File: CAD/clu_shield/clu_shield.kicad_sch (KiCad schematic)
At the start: 38 parts, among them J1 Conn_01x28_Pin, J2 Conn_01x02_Pin, J3 Conn_01x02_Pin, SW1 ERD516RSZ, SW10 SW_SPDT, SW11 SW_SPDT, SW12 SW_SPDT, SW13 SW_SPDT, SW2 ERD516RSZ, SW3 ERD516RSZ, SW4 ERD516RSZ, SW5 ERD508RSZ, SW6 SW_SPDT, SW7 SW_SPDT, SW8 SW_SPDT, SW9 SW_SPDT

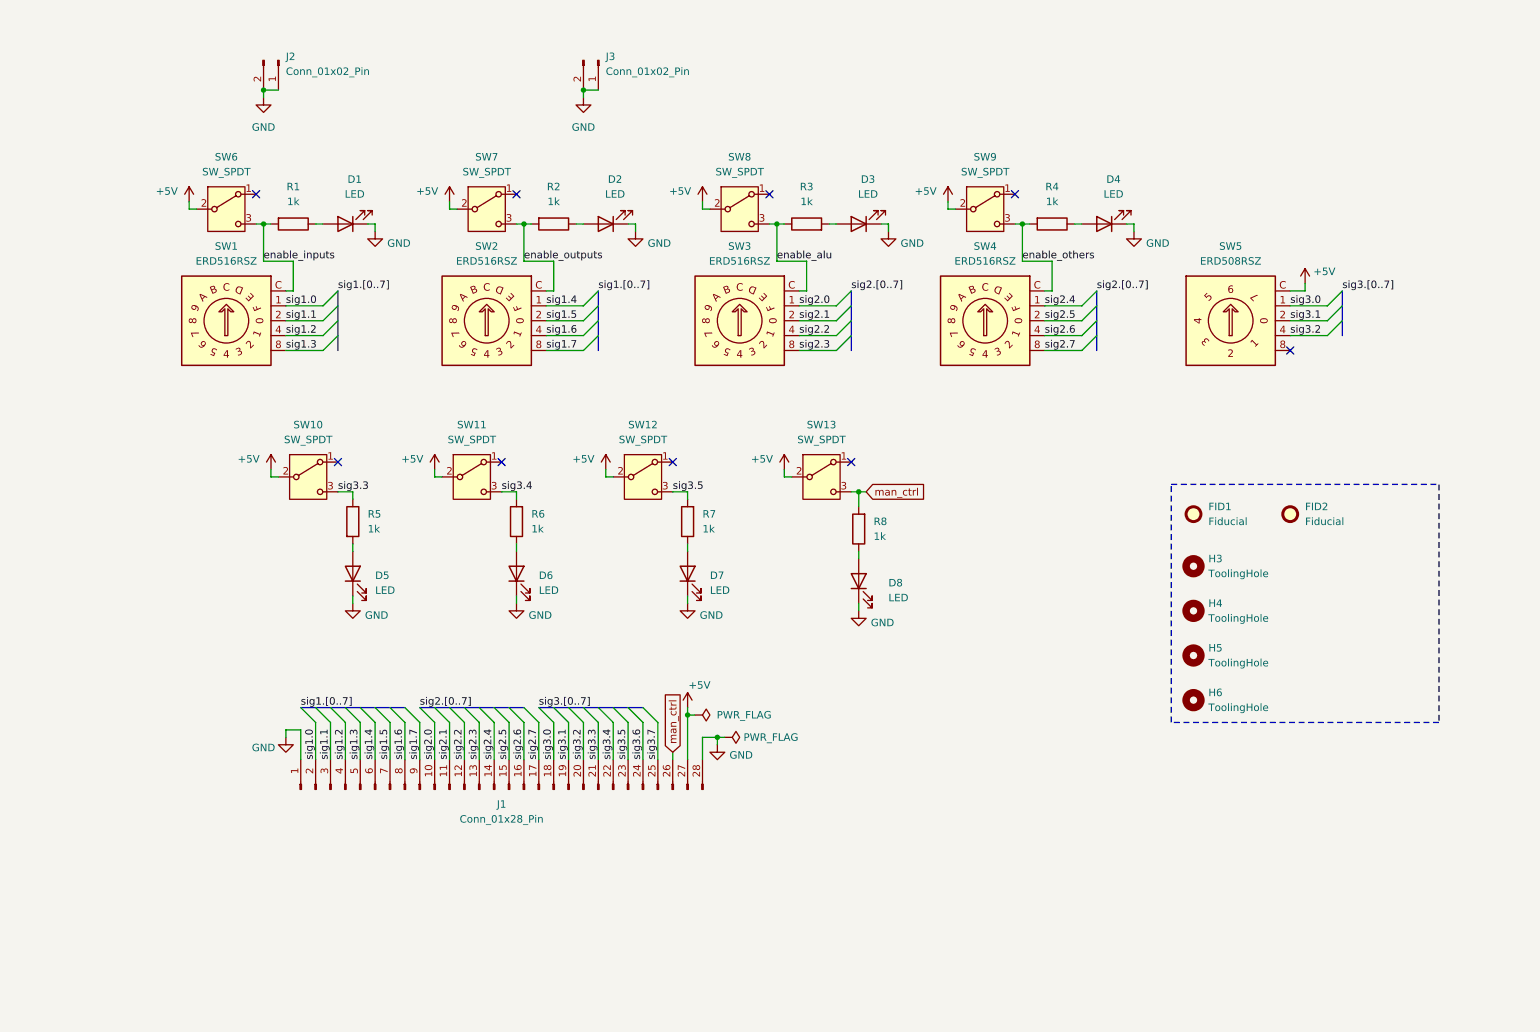
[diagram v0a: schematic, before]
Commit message: CLU Controls Shield layout changes, add reg2 select switch, CLU layout changes
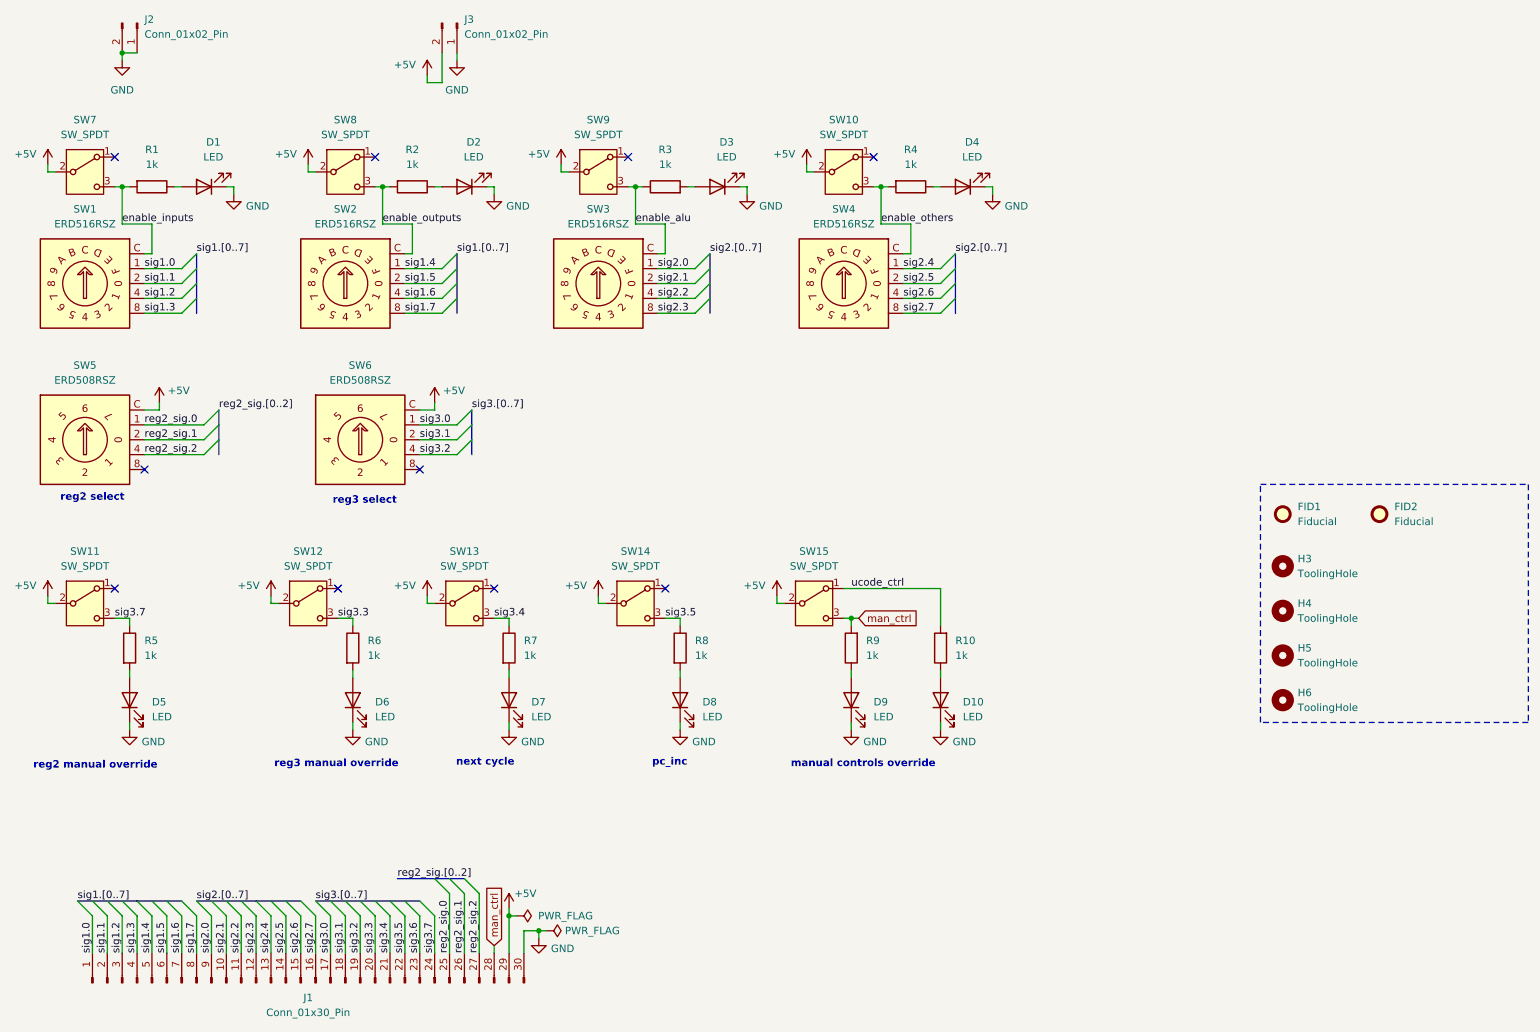
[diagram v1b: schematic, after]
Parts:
- removed J1: Conn_01x28_Pin, Connector_PinHeader_2.54mm:PinHeader_1x28_P2.54mm_Vertical, symbol Connector:Conn_01x28_Pin
- added D10, D5: LED, LED_SMD:LED_0805_2012Metric, symbol Device:LED
- added J1: Conn_01x30_Pin, Connector_PinHeader_2.54mm:PinHeader_1x30_P2.54mm_Vertical, symbol Connector:Conn_01x30_Pin
- added R10, R5: 1k, Resistor_SMD:R_0805_2012Metric, symbol Device:R
- added SW11: SW_SPDT, 8-bit_computer:SW_Slide_SPDT_8.5x3.8mm, symbol Switch:SW_SPDT
- added SW5: ERD508RSZ, 8-bit_computer:ERD5XXXS, symbol 8bit_computer:ERD508RSZ
- renumbered D5 to D6, D6 to D7, D7 to D8, D8 to D9, R5 to R6, R6 to R7, R7 to R8, R8 to R9, SW9 to SW10, SW10 to SW12, SW11 to SW13, SW12 to SW14, SW13 to SW15, SW5 to SW6, SW6 to SW7, SW7 to SW8, SW8 to SW9
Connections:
- net +5V: now also J3.2 (Pin_2), J1.29 (Pin_29), SW11.2 (B), SW5.C
- net GND: now also D10.1 (K), D5.1 (K), J1.30 (Pin_30); no longer J3.2 (Pin_2)
- net man_ctrl: now also J1.28 (Pin_28)
- net sig1.0: now also J1.1 (Pin_1)
- net sig1.1: now also J1.2 (Pin_2)
- net sig1.2: now also J1.3 (Pin_3)
- net sig1.3: now also J1.4 (Pin_4)
- net sig1.4: now also J1.5 (Pin_5)
- net sig1.5: now also J1.6 (Pin_6)
- net sig1.6: now also J1.7 (Pin_7)
- net sig1.7: now also J1.8 (Pin_8)
- net sig2.0: now also J1.9 (Pin_9)
- net sig2.1: now also J1.10 (Pin_10)
- net sig2.2: now also J1.11 (Pin_11)
- net sig2.3: now also J1.12 (Pin_12)
- net sig2.4: now also J1.13 (Pin_13)
- net sig2.5: now also J1.14 (Pin_14)
- net sig2.6: now also J1.15 (Pin_15)
- net sig2.7: now also J1.16 (Pin_16)
- net sig3.0: now also J1.17 (Pin_17)
- net sig3.1: now also J1.18 (Pin_18)
- net sig3.2: now also J1.19 (Pin_19)
- net sig3.3: now also J1.20 (Pin_20)
- net sig3.4: now also R7.1, J1.21 (Pin_21); no longer R7.2
- net sig3.5: now also R8.1, J1.22 (Pin_22); no longer R8.2
- net sig3.6: now also J1.23 (Pin_23)
- net sig3.7: now also J1.24 (Pin_24), R5.1, SW11.3 (C)
- net at D7.2 (A): now also R7.2; no longer R7.1
- net at D8.2 (A): now also R8.2; no longer R8.1
- net ucode_ctrl: now reaches SW15.1 (A)
- net ucode_ctrl: now also R10.2
- new net: D5.2 (A), R5.2
- new net: D10.2 (A), R10.1
- new net reg2_sig.0: J1.25 (Pin_25), SW5.1
- new net reg2_sig.1: J1.26 (Pin_26), SW5.2
- new net reg2_sig.2: J1.27 (Pin_27), SW5.4
- no-connect marks 9 -> 10
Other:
- note added: "manual controls override"
- note added: "next cycle"
- note added: "pc_inc"
- note added: "reg2 manual override"
- note added: "reg2 select"
- note added: "reg3 manual override"
- note added: "reg3 select"
- moved on the sheet: D1, D2, D3, D4, D6, D7, D8, D9, FID1, FID2, H3, H4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
